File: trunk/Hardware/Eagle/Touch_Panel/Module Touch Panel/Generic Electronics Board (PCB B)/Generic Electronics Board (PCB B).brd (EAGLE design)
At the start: 45.6 x 38.6 mm, 41 parts, among them IC1 ST3485, U1 XMEGA-A4TQFP, U2 SPX1117M3-L-3-3, X1 RJ45-8L-B, X6 RJ45-8L-B

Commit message: Work in progress
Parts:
- added D1: (no value), diode:DO-214AC
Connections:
- net +12V: now also D1.C
- net BUS_PWR: now also D1.A
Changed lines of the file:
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@@
 <element name="C16" library="rcl" package="C1206" value="100n" x="67.26" y="39.33"/>
 <element name="C17" library="rcl" package="C1206" value="100n" x="65.75" y="43.73" rot="R270"/>
+<element name="D1" library="diode" package="DO-214AC" value="" x="102.87" y="78.74" rot="R180"/>
 </elements>
 <signals>
@@
 <wire x1="100.61" y1="63.08" x2="100.6" y2="66.49" width="0" layer="19" extent="1-1"/>
 <wire x1="100.46" y1="60.45" x2="100.61" y2="63.08" width="0" layer="19" extent="1-1"/>
-<wire x1="68.4" y1="44.79" x2="100.46" y2="60.45" width="0" layer="19" extent="1-1"/>
-<wire x1="71.4" y1="41.45" x2="68.4" y2="44.79" width="0" layer="19" extent="1-1"/>
-<wire x1="74.38" y1="40.31" x2="71.4" y2="41.45" width="0" layer="19" extent="1-16"/>
+<wire x1="74.38" y1="40.31" x2="100.46" y2="60.45" width="0" layer="19" extent="1-16"/>
+<wire x1="71.4" y1="41.45" x2="74.38" y2="40.31" width="0" layer="19" extent="1-16"/>
 <wire x1="68.66" y1="39.33" x2="71.4" y2="41.45" width="0" layer="19" extent="1-1"/>
 <wire x1="67.78" y1="36.11" x2="68.66" y2="39.33" width="0" layer="19" extent="1-16"/>
 <wire x1="65.75" y1="42.33" x2="68.66" y2="39.33" width="0" layer="19" extent="1-1"/>
 <wire x1="62.78" y1="43.51" x2="65.75" y2="42.33" width="0" layer="19" extent="1-16"/>
+<wire x1="68.4" y1="44.79" x2="65.75" y2="42.33" width="0" layer="19" extent="1-1"/>
 <wire x1="67.78" y1="47.71" x2="68.4" y2="44.79" width="0" layer="19" extent="1-16"/>
 <wire x1="66.245" y1="50.98" x2="67.78" y2="47.71" width="0" layer="19" extent="1-16"/>
@@
 <wire x1="105.61" y1="63.08" x2="102.8954" y2="69.2404" width="0" layer="19" extent="1-1"/>
 <wire x1="103.26" y1="60.45" x2="105.61" y2="63.08" width="0" layer="19" extent="1-1"/>
-<wire x1="74.38" y1="39.51" x2="103.26" y2="60.45" width="0" layer="19" extent="1-16"/>
-<wire x1="71.4" y1="38.65" x2="74.38" y2="39.51" width="0" layer="19" extent="1-16"/>
-<wire x1="66.98" y1="36.11" x2="71.4" y2="38.65" width="0" layer="19" extent="1-16"/>
-<wire x1="65.86" y1="39.33" x2="66.98" y2="36.11" width="0" layer="19" extent="1-16"/>
-<wire x1="65.75" y1="45.13" x2="65.86" y2="39.33" width="0" layer="19" extent="1-1"/>
+<wire x1="71.2" y1="44.79" x2="103.26" y2="60.45" width="0" layer="19" extent="1-1"/>
+<wire x1="68.58" y1="47.71" x2="71.2" y2="44.79" width="0" layer="19" extent="1-16"/>
+<wire x1="65.75" y1="45.13" x2="68.58" y2="47.71" width="0" layer="19" extent="1-16"/>
 <wire x1="62.78" y1="44.31" x2="65.75" y2="45.13" width="0" layer="19" extent="1-16"/>
-<wire x1="71.2" y1="44.79" x2="65.75" y2="45.13" width="0" layer="19" extent="1-1"/>
-<wire x1="68.58" y1="47.71" x2="71.2" y2="44.79" width="0" layer="19" extent="1-16"/>
+<wire x1="65.86" y1="39.33" x2="65.75" y2="45.13" width="0" layer="19" extent="1-1"/>
+<wire x1="66.98" y1="36.11" x2="65.86" y2="39.33" width="0" layer="19" extent="1-16"/>
+<wire x1="71.4" y1="38.65" x2="66.98" y2="36.11" width="0" layer="19" extent="1-16"/>
+<wire x1="74.38" y1="39.51" x2="71.4" y2="38.65" width="0" layer="19" extent="1-16"/>
 <wire x1="65.665" y1="56.08" x2="68.58" y2="47.71" width="0" layer="19" extent="16-16"/>
 <wire x1="22.54" y1="60.96" x2="65.665" y2="56.08" width="0" layer="19" extent="1-16"/>
@@
 <contactref element="X6" pad="7"/>
 <contactref element="X1" pad="7"/>
+<contactref element="D1" pad="A"/>
+<wire x1="85.595" y1="26.54" x2="100.845" y2="78.74" width="0" layer="19" extent="1-1"/>
 <wire x1="57.655" y1="27.04" x2="85.595" y2="26.54" width="0" layer="19" extent="1-1"/>
 </signal>
@@
 <contactref element="U2" pad="3"/>
 <contactref element="C5" pad="+"/>
+<contactref element="D1" pad="C"/>
+<wire x1="104.31" y1="72.75" x2="104.895" y2="78.74" width="0" layer="19" extent="1-1"/>
 <wire x1="105.1814" y1="69.2404" x2="104.31" y2="72.75" width="0" layer="19" extent="1-1"/>
 <wire x1="105.6" y1="66.49" x2="105.1814" y2="69.2404" width="0" layer="19" extent="1-1"/>

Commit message: Touch Panel PCB_A & PCB_B final version (to electrical&part check)
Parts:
- removed C8, C9: 22n, rcl:C1206
- removed R48: 330R, rcl:M0805
- added JP6: (no value), pinhead:2X3SMD
- added R15, R16, R17, R18: 470k, rcl:R0603
- added R19, R20, R21, R22, R3, R4: 1k, rcl:R0603
- C1, C2, C4, C7: value 22n -> 4n7; device rcl:C1206 -> rcl:C0603
- C10, C12, C15, C16, C17, C6: device rcl:C1206 -> rcl:C0603
- C3: device rcl:C0805 -> rcl:C0603
- JP2, JP3, JP4, JP5: device pinhead:2X2SMD -> pinhead:2X02
- R1, R11, R12, R14, R2, R8: value 10k -> 1k; device rcl:R1206 -> rcl:R0603
- R10, R13, R5, R6, R7, R9: device rcl:M0805 -> rcl:R0603
- moved C4 76.0 mm to (80.9, 45.5), flipped to the bottom, turned to 270 degrees
- moved C7 70.6 mm to (79.4, 45.5), flipped to the bottom, turned to 270 degrees
- moved R8 64.9 mm to (71.6, 33.0), flipped to the bottom, turned to 270 degrees
- moved R11 59.5 mm to (70.2, 33.0), flipped to the bottom, turned to 270 degrees
- moved IC1 56.4 mm to (54.9, 35.5), turned to 90 degrees
- moved R12 54.3 mm to (68.7, 33.0), flipped to the bottom, turned to 270 degrees
- moved R1 52.7 mm to (77.3, 38.8)
- moved R10 51.1 mm to (56.6, 30.9), turned to 90 degrees
- moved R14 49.4 mm to (67.2, 33.0), flipped to the bottom, turned to 270 degrees
- moved R2 47.8 mm to (77.3, 37.3)
- moved R6 47.8 mm to (49.5, 35.8)
- moved C1 47.4 mm to (78.1, 45.5), flipped to the bottom, turned to 270 degrees
- moved R7 46.3 mm to (55.0, 30.9), turned to 90 degrees
- moved C3 43.0 mm to (48.7, 38.2), turned to 270 degrees
- moved D3 42.9 mm to (56.9, 49.5), turned to 180 degrees
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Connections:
- removed net JP1: R11.2
- removed net JP2: R12.2
- removed net JP3: R14.2
- removed net JP4: R2.2
- removed net JP5: R1.2
- removed net JP6: R8.2
- removed net N$16: IC1.2, R48.2
- removed net N$26: C8.1, R12.1, U1.15
- removed net N$27: C1.2, U1.42
- removed net N$28: C7.1, R11.1, U1.13
- removed net N$29: C4.2, U1.44
- new net CLK/SCK: JP6.P6, U1.27
- new net LA/: JP6.P5, U1.26
- new net N$10: R8.1, U1.14
- new net N$11: R11.1, U1.15
- new net N$12: R12.1, U1.16
- new net N$19: C1.2, R20.1, U1.5
- new net N$22: C4.2, R22.1, U1.7
- new net N$23: C7.1, R16.2, U1.44
- new net N$24: C4.1, R15.2, U1.43
- new net N$25: R15.1, R16.1, R17.1, R18.1, U1.42
- new net N$9: R4.1, U1.13
- new net OPTO: JP3.1, U1.41
- new net SDI/MOSI: JP6.P4, U1.25
- new net X5: JP5.4, R11.2
- new net X6: JP5.3, R12.2
- new net X7: JP5.1, R14.2
- new net Y3: JP3.4, R19.2
- net +3V3: now also JP6.P2
- net GND: now also JP6.P1, U1.3; no longer JP3.1, R48.1
- net N$1: now also R1.1, U1.10; no longer C2.2, U1.40
- net N$13: now also R14.1, U1.17; no longer C2.1, R1.1, U1.41
- net N$17: now also C2.1, R18.2, U1.2; no longer C8.2, U1.14
- net N$18: now also C2.2, R19.1, U1.4; no longer C4.1, R2.1, U1.1
- net N$2: now also R2.1, U1.11; no longer C1.1, R8.1, U1.43
- net N$20: now also C1.1, R17.2, U1.1; no longer C7.2, U1.12
- net N$21: now also C7.2, R21.1, U1.6; no longer C9.1, R14.1, U1.17
- net N$3: now also R3.1, U1.12; no longer C9.2, U1.16
- net N$6: now also IC1.2
- net X0: now also R1.2
- net X1: now also R2.2
- net X2: now also R3.2
- net X3: now also JP4.1, R4.2; no longer JP5.2
- net X4: now also JP5.2, R8.2; no longer JP5.4
- net Y0: now also R22.2
- net Y1: now also R21.2
- net Y2: now also R20.2
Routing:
- net GND: track 0.00 -> 175.1 mm, vias 0 -> 8
- net +3V3: track 0.00 -> 110.7 mm, vias 0 -> 7
- net BUS_PWR: track 0.00 -> 76.0 mm
- net GND_RS485: track 0.00 -> 36.0 mm
- net RS485_B: track 0.00 -> 35.3 mm
- net RS485_A: track 0.00 -> 34.7 mm
- net RS485_A2: track 0.00 -> 33.6 mm, vias 0 -> 2
- net X1: track 0.00 -> 32.3 mm, vias 0 -> 1
- net Y2: track 0.00 -> 30.5 mm
- net N$14: track 0.00 -> 30.0 mm, vias 0 -> 2
- net X0: track 0.00 -> 25.8 mm, vias 0 -> 1
- net X3: track 0.00 -> 25.6 mm, vias 0 -> 1
- net X2: track 0.00 -> 24.4 mm, vias 0 -> 2
- net Y3: track 0.00 -> 22.7 mm
- net Y0: track 0.00 -> 18.6 mm
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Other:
- board size 45.6 x 38.6 mm -> 45.6 x 36.8 mm

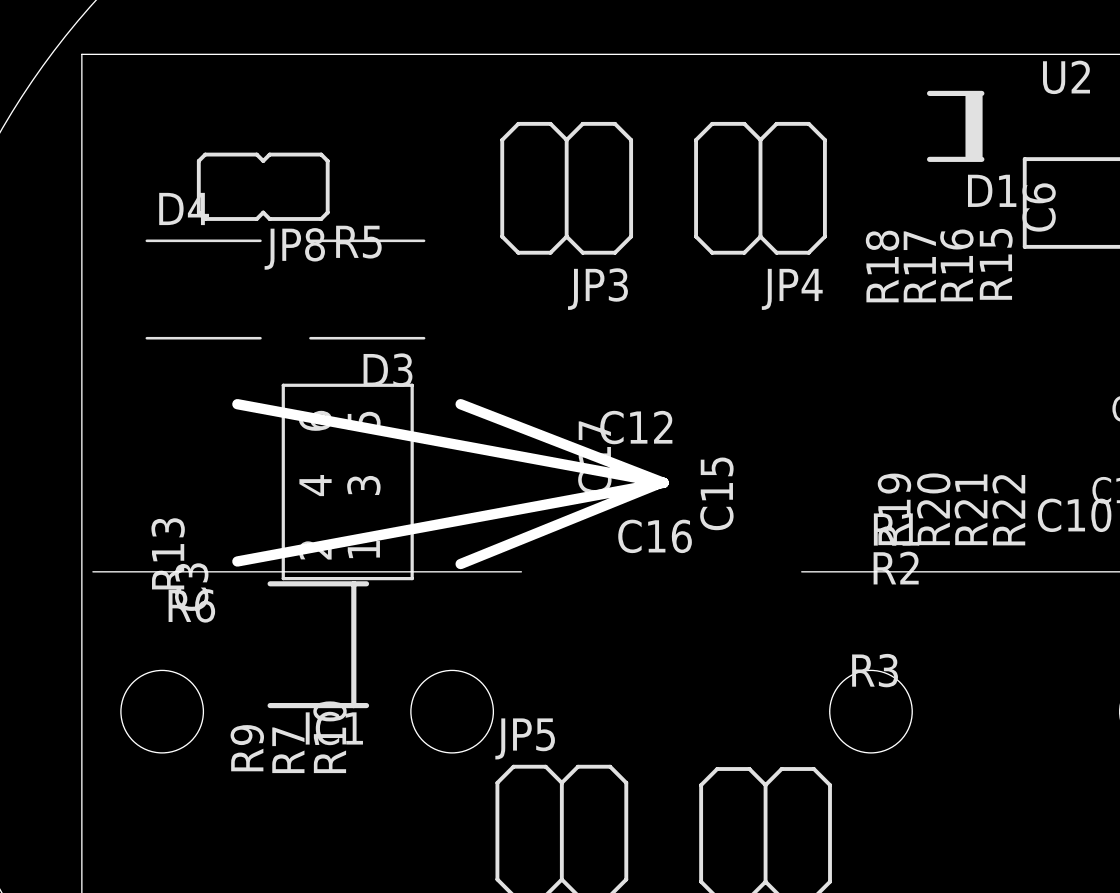
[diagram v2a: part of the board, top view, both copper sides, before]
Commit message: 
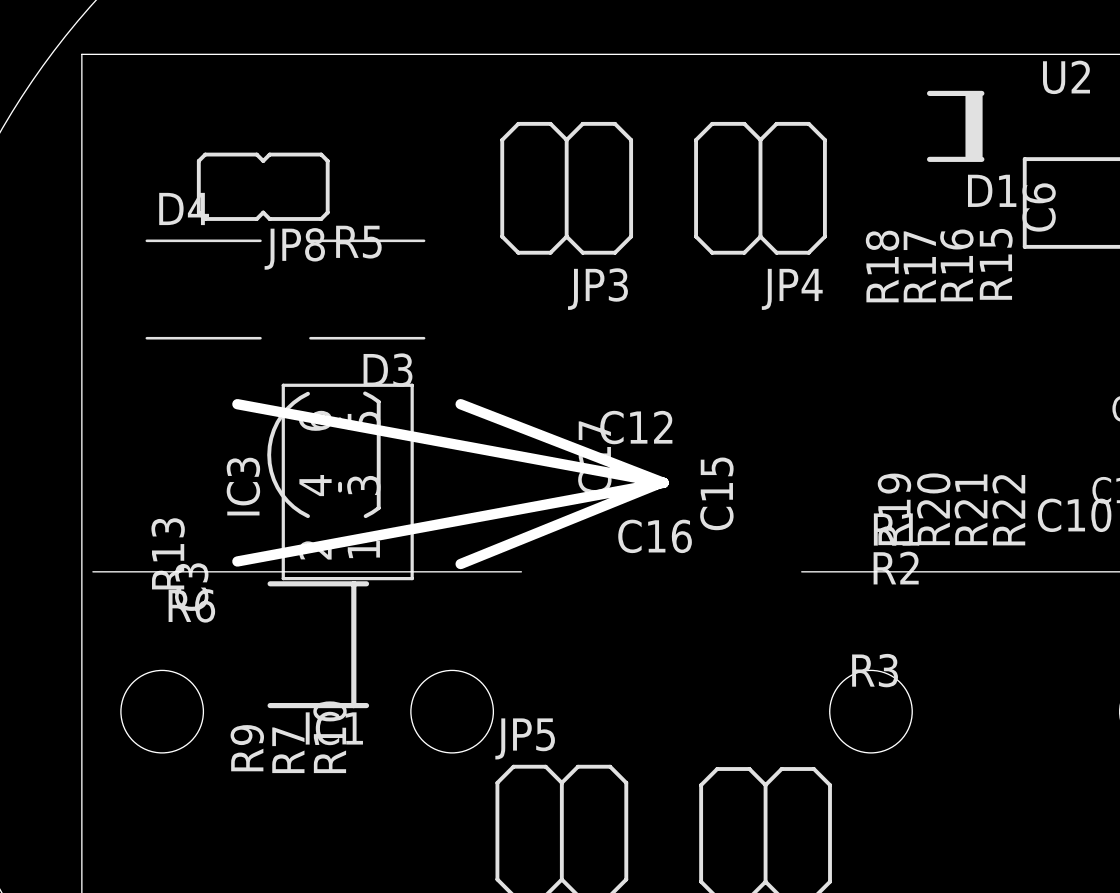
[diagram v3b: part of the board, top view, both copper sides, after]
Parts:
- added IC3: DS18B20, 1wire:TO92-
- added R23: 4k7, rcl:R0603
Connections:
- new net TEMP: IC3.2, R23.1, U1.28
- net +3V3: now also IC3.3, R23.2
- net GND: now also IC3.1
- net N$17: now also U1.43; no longer U1.2
- net N$20: now also U1.42; no longer U1.1
- net N$23: now also U1.41; no longer U1.44
- net N$24: now also U1.40; no longer U1.43
- net N$25: now also U1.44; no longer U1.42
- net OPTO: now also U1.1; no longer U1.41
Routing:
- net TEMP: track 0.00 -> 14.5 mm, vias 0 -> 1
- net N$14: track 30.0 -> 39.4 mm
- net +3V3: track 110.7 -> 119.6 mm
- net OPTO: track 8.82 -> 15.0 mm, vias 0 -> 2
- net CLK/SCK: track 14.4 -> 19.1 mm
- net N$24: track 15.0 -> 18.6 mm
- net N$23: track 11.7 -> 15.3 mm
- net N$20: track 9.31 -> 12.3 mm
- net N$17: track 7.58 -> 10.1 mm
- net N$25: track 12.6 -> 10.7 mm
- net LA/: track 6.60 -> 8.56 mm
- net GND: track 175.1 -> 176.5 mm
- net X2: track 24.4 -> 25.3 mm

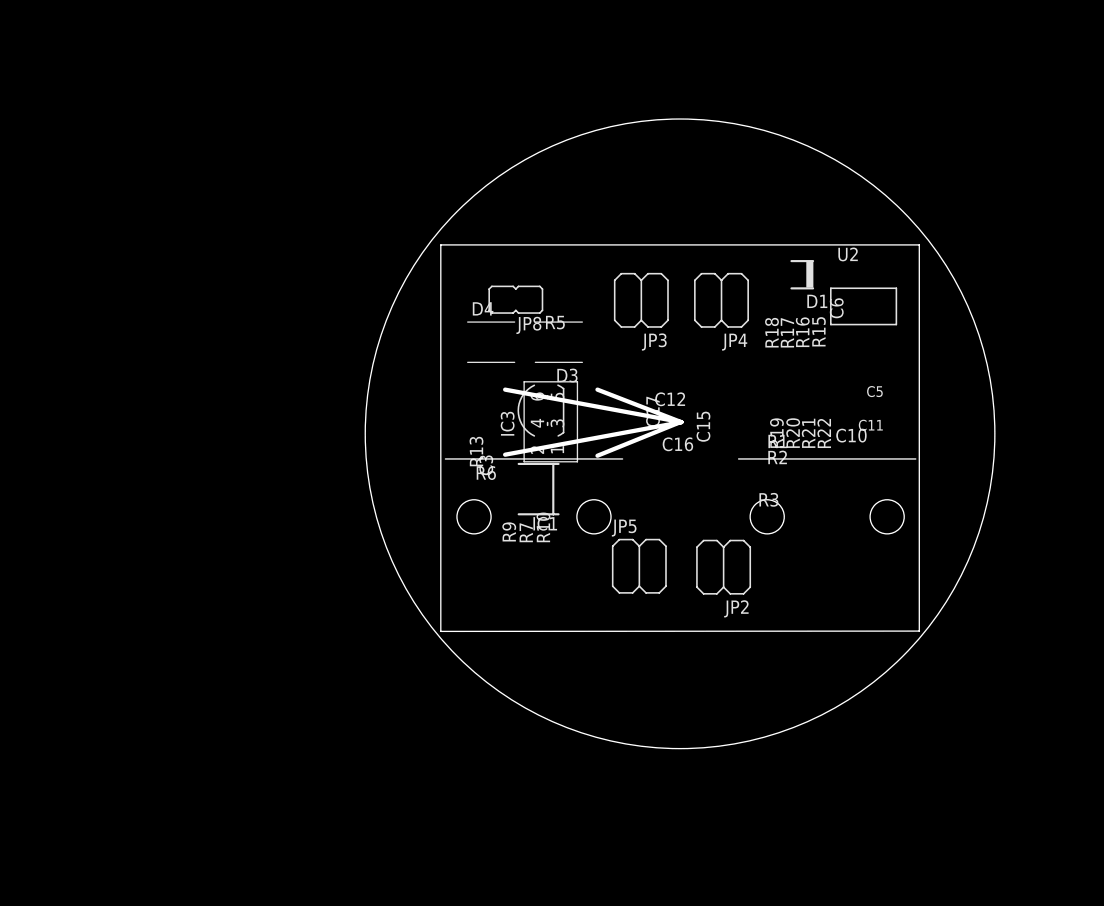
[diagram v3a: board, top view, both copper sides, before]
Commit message: Touch Panel (PCBA+PCBB) ver. 1.00
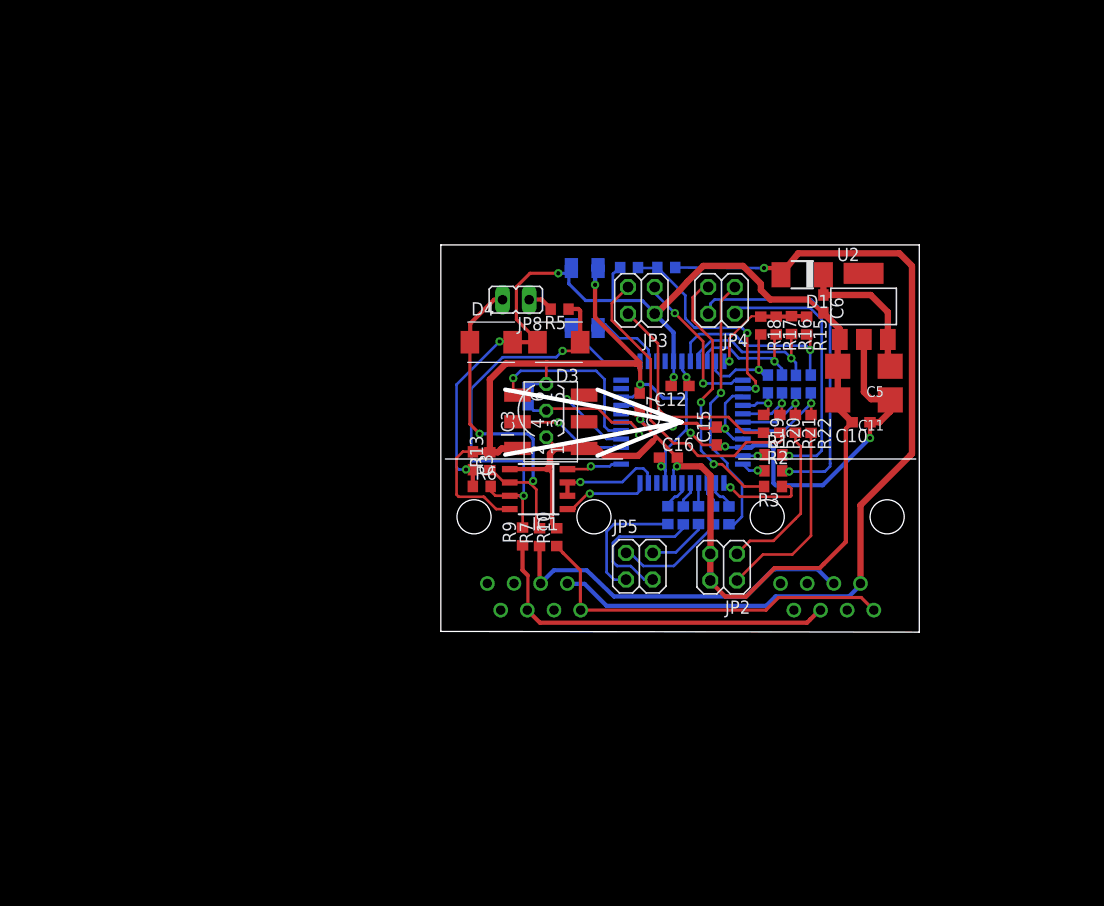
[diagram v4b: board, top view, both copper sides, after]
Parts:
- added R24: 11k, rcl:R0603
- added R25: 100k, rcl:R0603
- moved R15 0.32 mm to (80.5, 51.1)
- moved R16 0.28 mm to (79.0, 51.2)
- moved R17 0.28 mm to (77.6, 51.1)
- moved R18 0.28 mm to (76.1, 51.1)
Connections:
- new net POWER_METER: R24.2, R25.1, U1.2
- net BUS_PWR: now also R25.2
- net GND: now also R24.1
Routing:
- net POWER_METER: track 0.00 -> 21.3 mm, vias 0 -> 2
- net BUS_PWR: track 76.0 -> 86.8 mm, vias 0 -> 1
- net GND: track 176.5 -> 179.5 mm
- net CLK/SCK: track 19.1 -> 17.7 mm
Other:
- board size 45.6 x 36.8 mm -> 45.6 x 36.9 mm
- board text added: "Generic Electronics Board (PCB B)"
- board text added: "ver. 1.00"
